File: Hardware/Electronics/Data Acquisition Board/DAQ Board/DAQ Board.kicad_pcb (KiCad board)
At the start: 4 copper layers, 94.7 x 58.9 mm, 158 parts, among them J1 Conn_01x09_Male, J2 USB_B_Mini, J3 Battery Connector, J4 DC Barrel Jack, J5 HC-05 BT Module, J6 ICSP Header, Q1 DMP2100U, SW1 DIP, SW10 SW_SPDT, SW11 SW_SPDT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

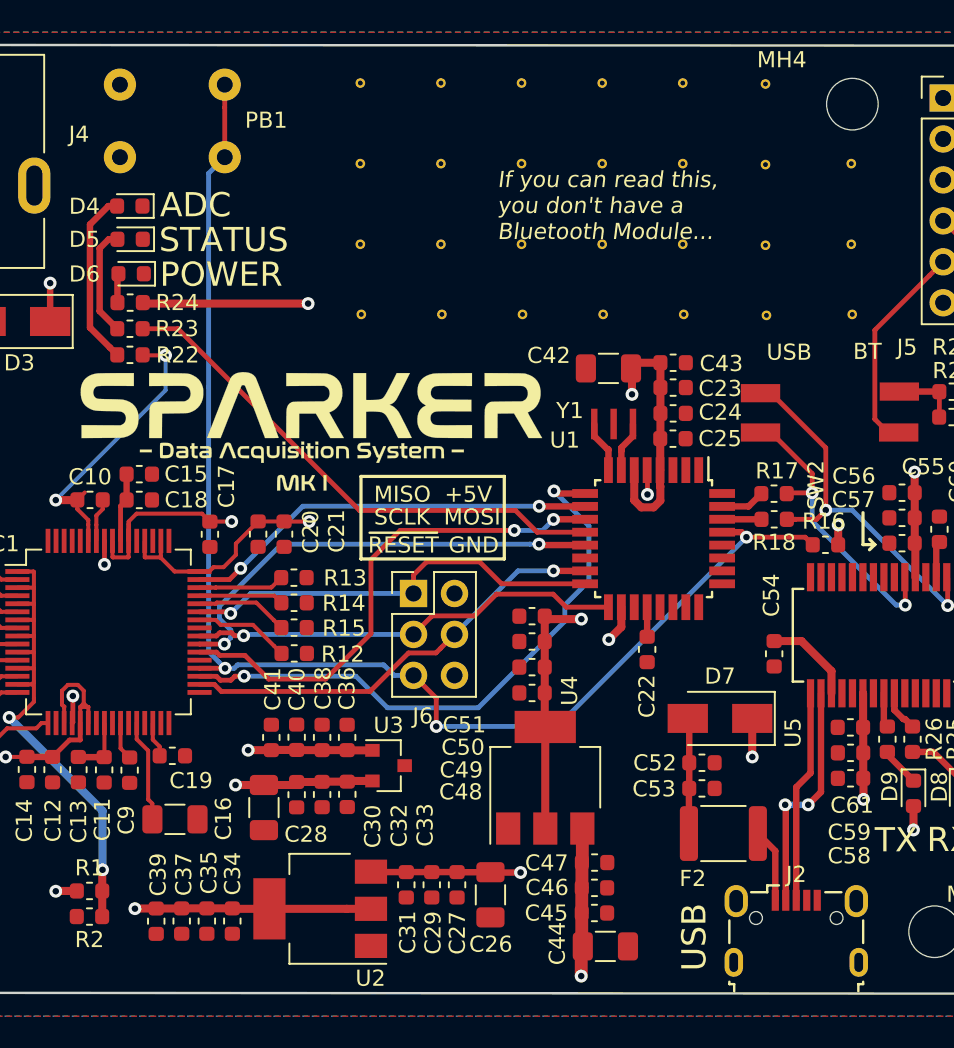
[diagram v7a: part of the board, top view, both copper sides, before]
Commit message: Routed new LDOs
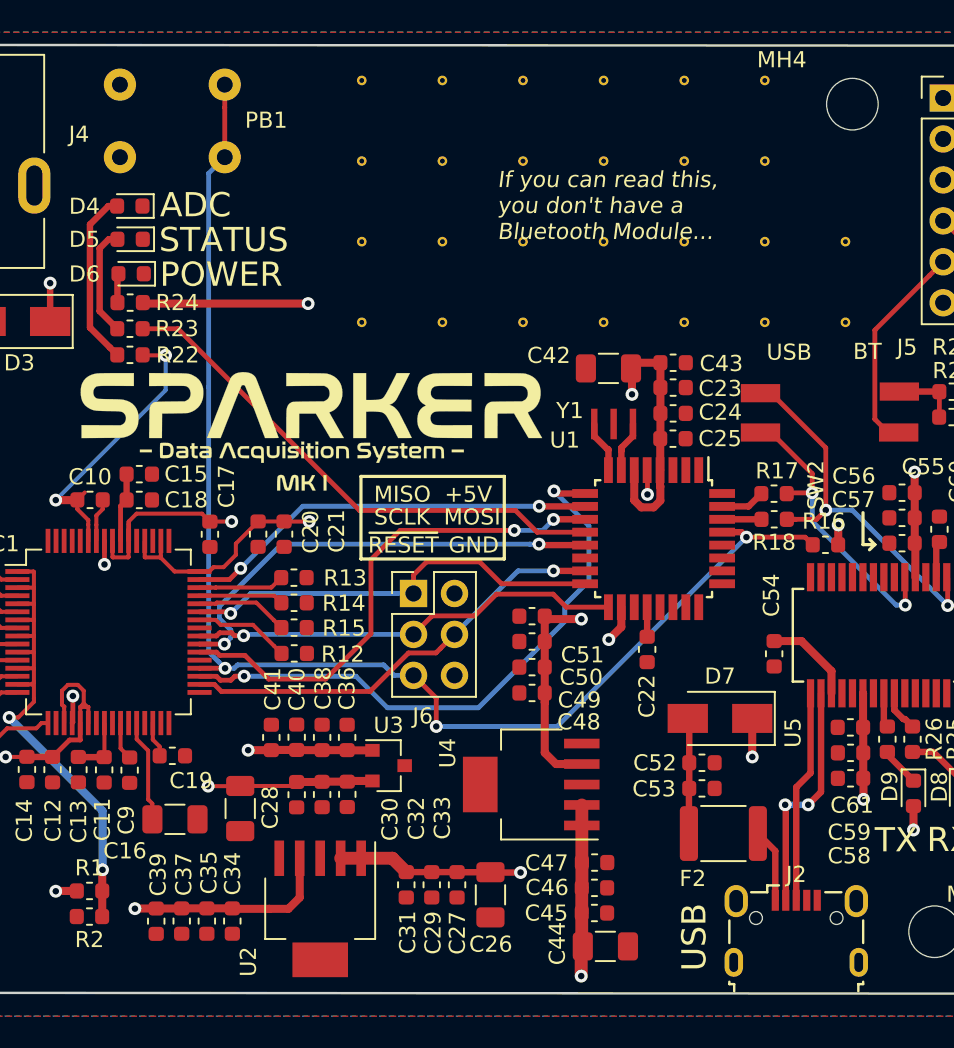
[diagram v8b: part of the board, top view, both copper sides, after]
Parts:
- removed the ? at (204.0, 85.3)
- removed the ? at (173.6, 85.3)
- removed the ? at (193.6, 85.3)
- removed the ? at (183.6, 85.3)
- removed the ? at (193.5, 81.0)
- removed the ? at (188.5, 81.0)
- removed the ? at (183.5, 81.0)
- removed the ? at (178.5, 81.0)
- removed the ? at (173.5, 81.0)
- removed the ? at (193.5, 76.0)
- removed the ? at (188.5, 76.0)
- removed the ? at (203.9, 81.0)
- removed the ? at (183.5, 76.0)
- removed the ? at (178.5, 76.0)
- removed the ? at (173.5, 76.0)
- removed the ? at (193.5, 71.0)
- removed the ? at (188.5, 71.0)
- removed the ? at (183.5, 71.0)
- removed the ? at (178.5, 71.0)
- removed the ? at (173.5, 71.0)
- removed the ? at (203.9, 76.0)
- removed the ? at (198.7, 85.4)
- removed the ? at (198.6, 71.0)
- removed the ? at (198.6, 81.0)
- removed the ? at (198.6, 76.0)
- removed the ? at (188.6, 85.3)
- removed the ? at (178.6, 85.3)
- added ?: , Vias:VIA-0.6mm, F.Cu at (203.6, 85.8)
- added ?: , Vias:VIA-0.6mm, F.Cu at (193.6, 80.8)
- added ?: , Vias:VIA-0.6mm, F.Cu at (188.6, 80.8)
- added ?: , Vias:VIA-0.6mm, F.Cu at (183.6, 80.8)
- added ?: , Vias:VIA-0.6mm, F.Cu at (178.6, 80.8)
- added ?: , Vias:VIA-0.6mm, F.Cu at (173.6, 80.8)
- added ?: , Vias:VIA-0.6mm, F.Cu at (198.6, 75.8)
- added ?: , Vias:VIA-0.6mm, F.Cu at (193.6, 75.8)
- added ?: , Vias:VIA-0.6mm, F.Cu at (188.6, 75.8)
- added ?: , Vias:VIA-0.6mm, F.Cu at (183.6, 75.8)
- added ?: , Vias:VIA-0.6mm, F.Cu at (178.6, 75.8)
- added ?: , Vias:VIA-0.6mm, F.Cu at (198.6, 85.8)
- added ?: , Vias:VIA-0.6mm, F.Cu at (173.6, 75.8)
- added ?: , Vias:VIA-0.6mm, F.Cu at (198.6, 70.8)
- added ?: , Vias:VIA-0.6mm, F.Cu at (193.6, 70.8)
- added ?: , Vias:VIA-0.6mm, F.Cu at (188.6, 70.8)
- added ?: , Vias:VIA-0.6mm, F.Cu at (183.6, 70.8)
- added ?: , Vias:VIA-0.6mm, F.Cu at (178.6, 70.8)
- added ?: , Vias:VIA-0.6mm, F.Cu at (173.6, 70.8)
- added ?: , Vias:VIA-0.6mm, F.Cu at (193.6, 85.8)
- added ?: , Vias:VIA-0.6mm, F.Cu at (188.6, 85.8)
- added ?: , Vias:VIA-0.6mm, F.Cu at (183.6, 85.8)
- added ?: , Vias:VIA-0.6mm, F.Cu at (178.6, 85.8)
- added ?: , Vias:VIA-0.6mm, F.Cu at (173.6, 85.8)
- added ?: , Vias:VIA-0.6mm, F.Cu at (203.6, 80.8)
- added ?: , Vias:VIA-0.6mm, F.Cu at (198.6, 80.8)
- U2, U4: value LM1117-5.0 -> MCP1755T-5002E_SOT223-5; footprint Package_TO_SOT_SMD:SOT-223 -> Package_TO_SOT_SMD:SOT-223-6
- moved C28 1.47 mm to (166.1, 116.0)
- moved U4 0.97 mm to (184.1, 114.5), turned to 180 degrees
- turned U2 to 270 degrees
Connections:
- U2 pad 1: /GND -> /VIN
- U2 pad 2: /ADC1299/AVDD -> /VIN
- U2 pad 3: /VIN -> /GND
- U4 pad 1: /GND -> /VIN
- U4 pad 2: /+5V -> /VIN
- U4 pad 3: /VIN -> /GND
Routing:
- net /VIN: track 24.1 -> 27.8 mm
- net /+5V: track 63.9 -> 61.8 mm
